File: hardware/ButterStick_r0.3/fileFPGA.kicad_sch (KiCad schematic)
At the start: 20 parts, among them U2 ECP5UM5G_85_CABGA381, U6 S25FL127S, X1 ASDMB

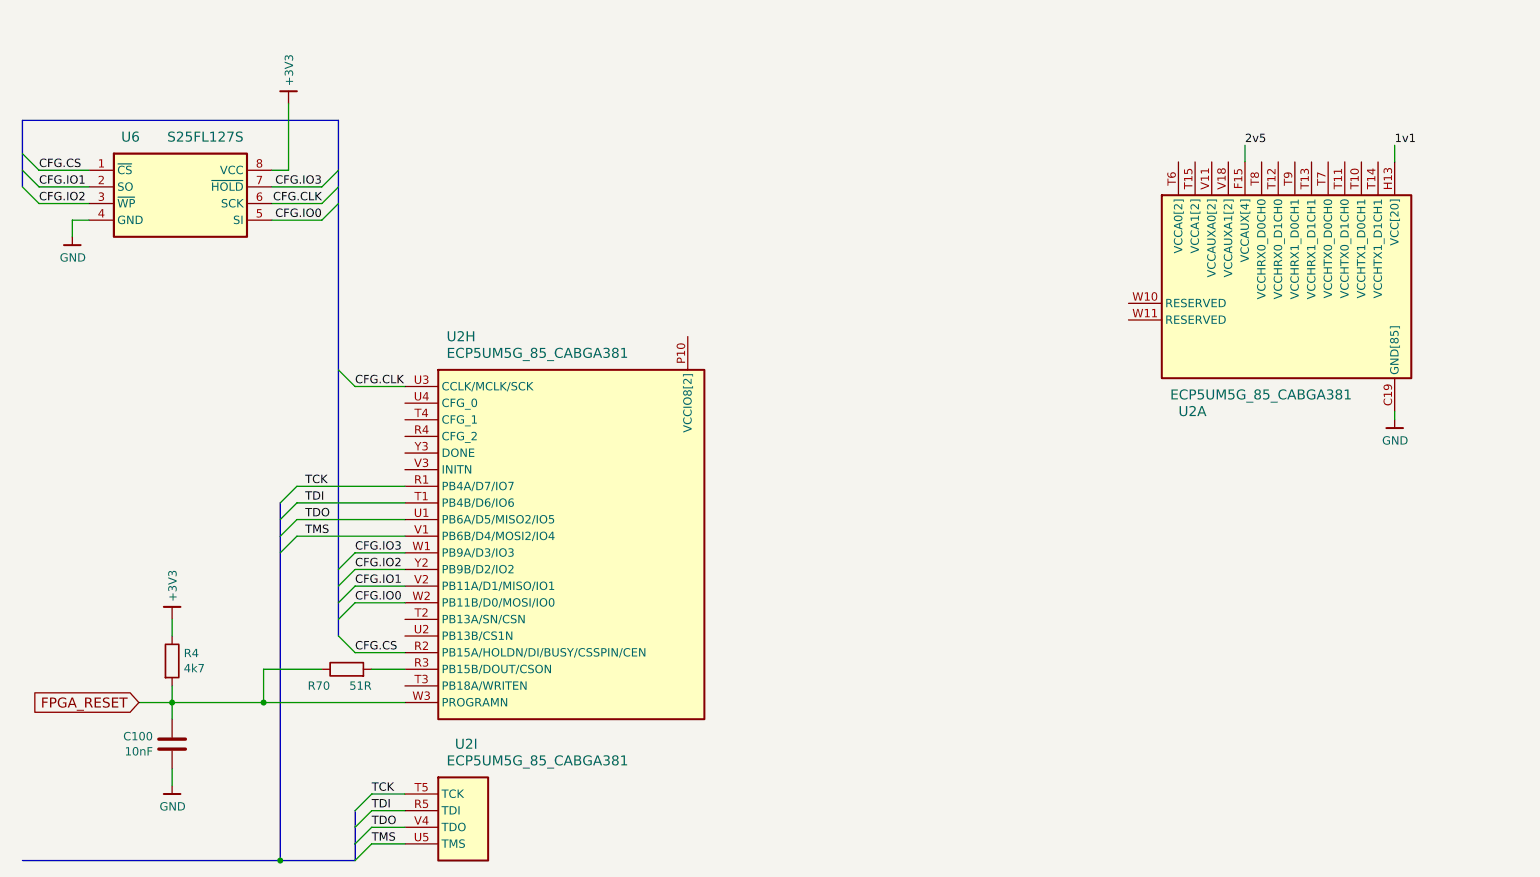
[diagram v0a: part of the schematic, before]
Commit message: hw.r0_3: routing improvements
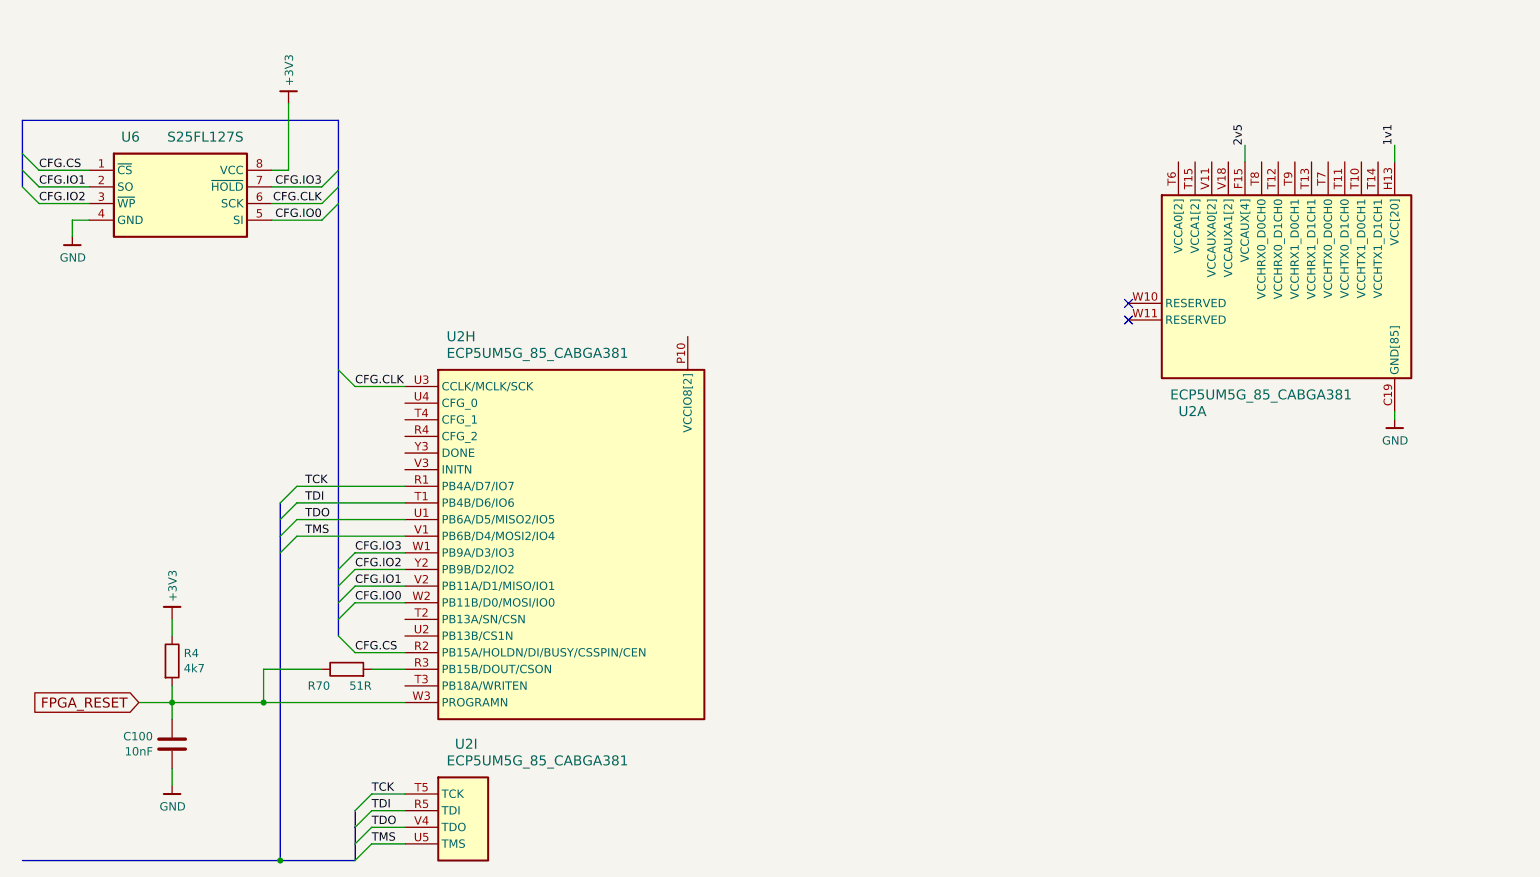
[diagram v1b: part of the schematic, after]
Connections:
- no-connect marks 0 -> 2
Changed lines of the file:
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@@
   (junction (at 502.92 -36.83))
   (junction (at 66.04 166.37))
+  (no_connect (at 195.58 81.28))
+  (no_connect (at 195.58 83.82))
   (bus_entry (at 29.21 60.96) (size -2.54 -2.54))
   (bus_entry (at 29.21 63.5) (size -2.54 -2.54))
@@
   (wire (pts (xy 502.92 -41.91) (xy 502.92 -36.83)))
   (wire (pts (xy 502.92 -36.83) (xy 502.92 -35.56)))
-  (bus (pts (xy 26.67 53.34) (xy 26.67 60.96)))
-  (bus (pts (xy 26.67 60.96) (xy 26.67 63.5)))
+  (bus (pts (xy 26.67 53.34) (xy 26.67 58.42)))
+  (bus (pts (xy 26.67 58.42) (xy 26.67 63.5)))
   (bus (pts (xy 26.67 166.37) (xy 66.04 166.37)))
   (bus (pts (xy 66.04 111.76) (xy 66.04 116.84)))
@@
   (bus (pts (xy 74.93 53.34) (xy 74.93 63.5)))
   (bus (pts (xy 74.93 63.5) (xy 74.93 91.44)))
-  (bus (pts (xy 74.93 91.44) (xy 74.93 121.92)))
-  (bus (pts (xy 74.93 121.92) (xy 74.93 127)))
-  (bus (pts (xy 74.93 127) (xy 74.93 132.08)))
-  (bus (pts (xy 77.47 158.75) (xy 77.47 163.83)))
-  (bus (pts (xy 77.47 163.83) (xy 77.47 166.37)))
+  (bus (pts (xy 74.93 91.44) (xy 74.93 124.46)))
+  (bus (pts (xy 74.93 124.46) (xy 74.93 129.54)))
+  (bus (pts (xy 74.93 129.54) (xy 74.93 132.08)))
+  (bus (pts (xy 77.47 158.75) (xy 77.47 161.29)))
+  (bus (pts (xy 77.47 161.29) (xy 77.47 166.37)))
   (text "LEDS/SDMMC\n" (at 307.34 -17.78 90)
     (effects (font (size 2.54 2.54)) (justify left bottom))
@@
     (effects (font (size 1.27 1.27)) (justify left bottom))
   )
-  (label "2v5" (at 213.36 57.15 0)
-    (effects (font (size 1.27 1.27)) (justify left bottom))
-  )
-  (label "1v1" (at 236.22 57.15 0)
-    (effects (font (size 1.27 1.27)) (justify left bottom))
-  )
+  (label "2v5" (at 213.36 57.15 90)
+    (effects (font (size 1.27 1.27)) (justify left bottom))
+  )
+  (label "1v1" (at 236.22 57.15 90)
+    (effects (font (size 1.27 1.27)) (justify left bottom))
+  )

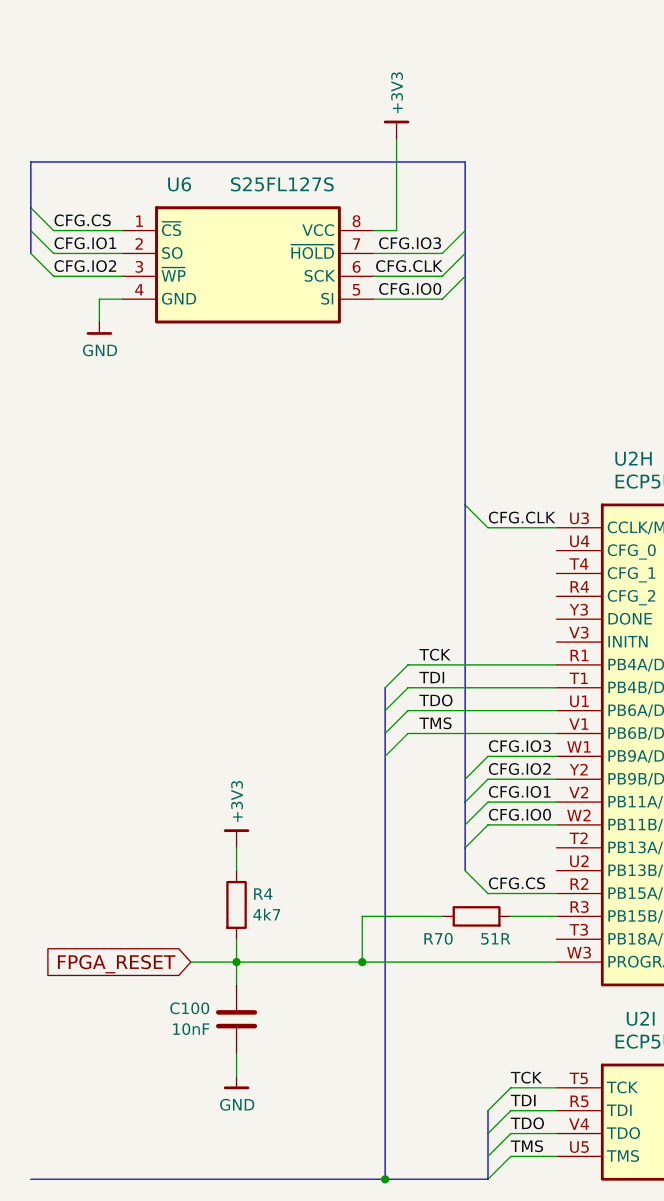
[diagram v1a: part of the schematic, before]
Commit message: hw.r0_3: Start routing DDR3 interface
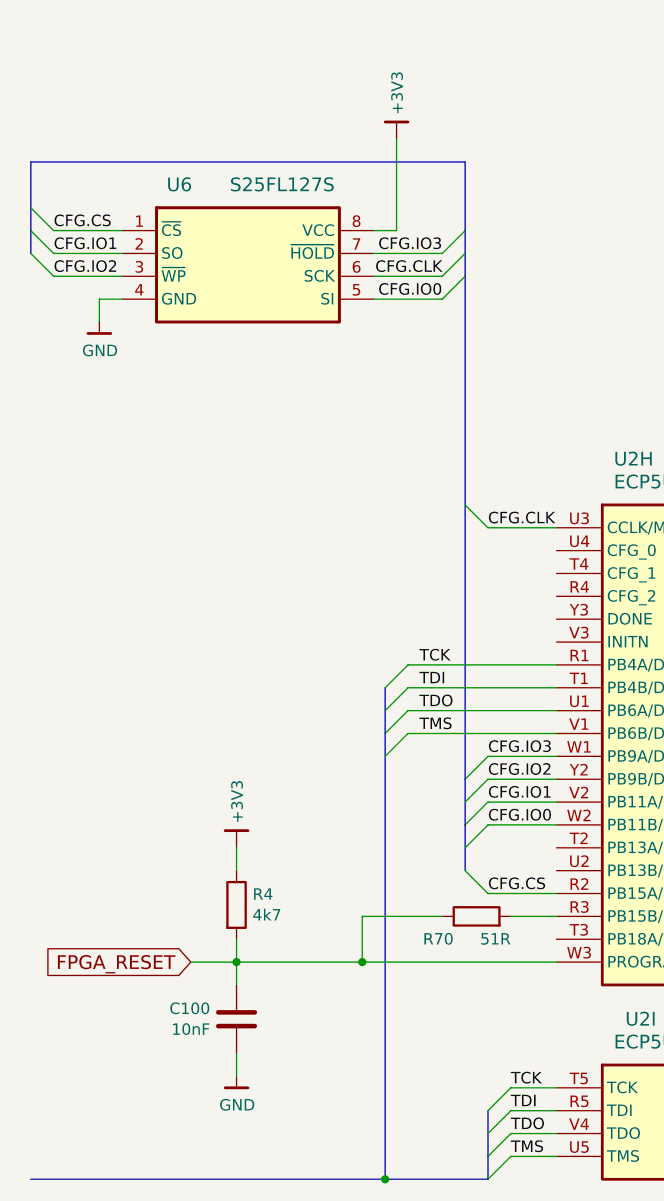
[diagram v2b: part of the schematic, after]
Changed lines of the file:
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@@
-(kicad_sch (version 20200512) (host eeschema "5.99.0-unknown-c8476d6~101~ubuntu18.04.1")
-  (page 8 20)
+(kicad_sch (version 20200512) (host eeschema "5.99.0-unknown-711fc99~101~ubuntu18.04.1")
+  (page 1 20)
   (paper "A4")
   (title_block
@@
   (wire (pts (xy 502.92 -41.91) (xy 502.92 -36.83)))
   (wire (pts (xy 502.92 -36.83) (xy 502.92 -35.56)))
-  (bus (pts (xy 26.67 53.34) (xy 26.67 58.42)))
-  (bus (pts (xy 26.67 58.42) (xy 26.67 63.5)))
+  (bus (pts (xy 26.67 53.34) (xy 26.67 60.96)))
+  (bus (pts (xy 26.67 60.96) (xy 26.67 63.5)))
   (bus (pts (xy 26.67 166.37) (xy 66.04 166.37)))
   (bus (pts (xy 66.04 111.76) (xy 66.04 116.84)))
@@
   (bus (pts (xy 66.04 166.37) (xy 77.47 166.37)))
   (bus (pts (xy 74.93 53.34) (xy 26.67 53.34)))
-  (bus (pts (xy 74.93 53.34) (xy 74.93 63.5)))
-  (bus (pts (xy 74.93 63.5) (xy 74.93 91.44)))
-  (bus (pts (xy 74.93 91.44) (xy 74.93 124.46)))
-  (bus (pts (xy 74.93 124.46) (xy 74.93 129.54)))
-  (bus (pts (xy 74.93 129.54) (xy 74.93 132.08)))
-  (bus (pts (xy 77.47 158.75) (xy 77.47 161.29)))
-  (bus (pts (xy 77.47 161.29) (xy 77.47 166.37)))
+  (bus (pts (xy 74.93 53.34) (xy 74.93 60.96)))
+  (bus (pts (xy 74.93 60.96) (xy 74.93 66.04)))
+  (bus (pts (xy 74.93 66.04) (xy 74.93 121.92)))
+  (bus (pts (xy 74.93 121.92) (xy 74.93 127)))
+  (bus (pts (xy 74.93 127) (xy 74.93 132.08)))
+  (bus (pts (xy 77.47 158.75) (xy 77.47 163.83)))
+  (bus (pts (xy 77.47 163.83) (xy 77.47 166.37)))
   (text "LEDS/SDMMC\n" (at 307.34 -17.78 90)
     (effects (font (size 2.54 2.54)) (justify left bottom))

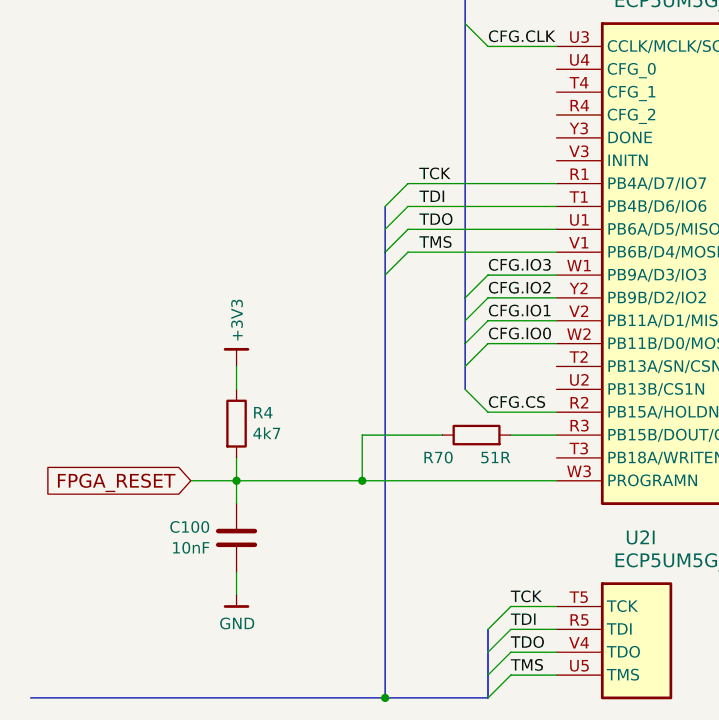
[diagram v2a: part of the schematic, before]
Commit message: hw.r0_3: routed SYZYGY, begin routing RGMII/ULPI
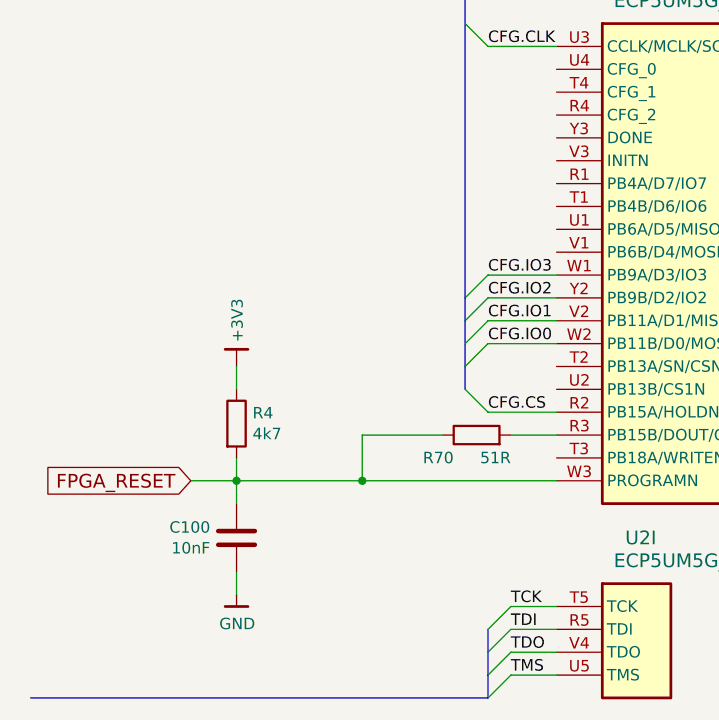
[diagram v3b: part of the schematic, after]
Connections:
- net TCK: no longer U2.R1 (PB4A/D7/IO7)
- net TDI: no longer U2.T1 (PB4B/D6/IO6)
- net TDO: no longer U2.U1 (PB6A/D5/MISO2/IO5)
- net TMS: no longer U2.V1 (PB6B/D4/MOSI2/IO4)
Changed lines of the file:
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@@
 (kicad_sch (version 20200512) (host eeschema "5.99.0-unknown-711fc99~101~ubuntu18.04.1")
-  (page 1 20)
+  (page 1 19)
   (paper "A4")
   (title_block
@@
   (junction (at 63.5 142.24))
   (junction (at 502.92 -36.83))
-  (junction (at 66.04 166.37))
   (no_connect (at 195.58 81.28))
   (no_connect (at 195.58 83.82))
@@
   (bus_entry (at 29.21 63.5) (size -2.54 -2.54))
   (bus_entry (at 29.21 66.04) (size -2.54 -2.54))
-  (bus_entry (at 66.04 111.76) (size 2.54 -2.54))
-  (bus_entry (at 66.04 114.3) (size 2.54 -2.54))
-  (bus_entry (at 66.04 116.84) (size 2.54 -2.54))
-  (bus_entry (at 66.04 119.38) (size 2.54 -2.54))
   (bus_entry (at 72.39 63.5) (size 2.54 -2.54))
   (bus_entry (at 72.39 66.04) (size 2.54 -2.54))
@@
   (wire (pts (xy 64.77 60.96) (xy 67.31 60.96)))
   (wire (pts (xy 67.31 60.96) (xy 67.31 50.8)))
-  (wire (pts (xy 68.58 109.22) (xy 85.09 109.22)))
-  (wire (pts (xy 68.58 111.76) (xy 85.09 111.76)))
-  (wire (pts (xy 68.58 114.3) (xy 85.09 114.3)))
-  (wire (pts (xy 68.58 116.84) (xy 85.09 116.84)))
   (wire (pts (xy 72.39 63.5) (xy 64.77 63.5)))
   (wire (pts (xy 72.39 66.04) (xy 64.77 66.04)))
@@
   (bus (pts (xy 26.67 53.34) (xy 26.67 60.96)))
   (bus (pts (xy 26.67 60.96) (xy 26.67 63.5)))
-  (bus (pts (xy 26.67 166.37) (xy 66.04 166.37)))
-  (bus (pts (xy 66.04 111.76) (xy 66.04 116.84)))
-  (bus (pts (xy 66.04 116.84) (xy 66.04 166.37)))
-  (bus (pts (xy 66.04 166.37) (xy 77.47 166.37)))
+  (bus (pts (xy 26.67 166.37) (xy 77.47 166.37)))
   (bus (pts (xy 74.93 53.34) (xy 26.67 53.34)))
   (bus (pts (xy 74.93 53.34) (xy 74.93 60.96)))
   (bus (pts (xy 74.93 60.96) (xy 74.93 66.04)))
   (bus (pts (xy 74.93 66.04) (xy 74.93 121.92)))
-  (bus (pts (xy 74.93 121.92) (xy 74.93 127)))
-  (bus (pts (xy 74.93 127) (xy 74.93 132.08)))
+  (bus (pts (xy 74.93 121.92) (xy 74.93 124.46)))
+  (bus (pts (xy 74.93 124.46) (xy 74.93 129.54)))
+  (bus (pts (xy 74.93 129.54) (xy 74.93 132.08)))
   (bus (pts (xy 77.47 158.75) (xy 77.47 163.83)))
   (bus (pts (xy 77.47 163.83) (xy 77.47 166.37)))
@@
     (effects (font (size 1.27 1.27)) (justify left bottom))
   )
-  (label "TCK" (at 69.85 109.22 0)
-    (effects (font (size 1.27 1.27)) (justify left bottom))
-  )
-  (label "TDI" (at 69.85 111.76 0)
-    (effects (font (size 1.27 1.27)) (justify left bottom))
-  )
-  (label "TDO" (at 69.85 114.3 0)
-    (effects (font (size 1.27 1.27)) (justify left bottom))
-  )
-  (label "TMS" (at 69.85 116.84 0)
-    (effects (font (size 1.27 1.27)) (justify left bottom))
-  )

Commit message: hw.r0_3: major blocks roughly routed
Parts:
- renumbered C100 to C20, C80 to C21, C81 to C22, C82 to C23, C83 to C24, C84 to C25, C85 to C26, C86 to C27, C87 to C28, C88 to C29, C89 to C30, C90 to C31, C91 to C32, R4 to R41, R70 to R42, R66 to R43, R47 to R44, U2 to U4, U6 to U5

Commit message: hw.r0d3: Length matched all SYZYGY ports
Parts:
- removed X1: ASDMB, Oscillators:Oscillator_SMD_SeikoEpson_SG210-4pin_2.5x2.0mm, symbol gkl_time:TYETBCSANF-32.000000
- added R45, R46, R47, R48, R49: 1K, Resistor_SMD:R_0402_1005Metric, symbol Device:R
- added TP1, TP2, TP3, TP4: TestPoint_Small, gkl_conn:TestPoint_Pad_D1.0mm, symbol Connector:TestPoint_Small
- R44: value 20R -> 1K; PN RMCF0402FT20R0 -> RC0402JR-074K7L; SN-DK (none) -> P10KDECT-ND
- renumbered R41 to R43, R42 to R50, R43 to R51
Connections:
- net PCLKT1_0 is gone; now on net CFG2: R44.2
- net +3V3: now also R44.1, U4.P10 (VCCIO8[2]), U4.P9 (VCCIO8[2]), R46.1, R48.1
- net GND: now also R45.2, R47.2, R49.2
- net TCK: now also TP4.1
- net TDI: now also TP3.1
- net TDO: now also TP2.1
- net TMS: now also TP1.1
- net CFG2: now reaches U4.R4 (CFG_2)
- net CFG2: now also R45.1
- net CFG1: now reaches U4.T4 (CFG_1)
- net CFG1: now also R46.2, R47.1
- net CFG0: now reaches U4.U4 (CFG_0)
- net CFG0: now also R48.2, R49.1
- net 1v1 renamed +1V1
- net 2v5 renamed +2V5
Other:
- moved on the sheet: U4A

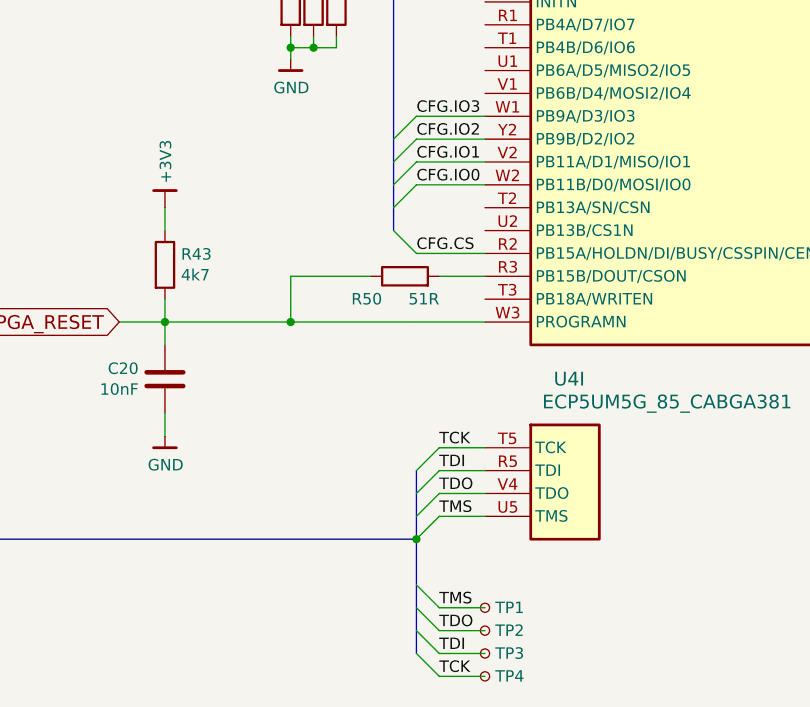
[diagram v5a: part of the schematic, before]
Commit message: hw.r0d3: update routing
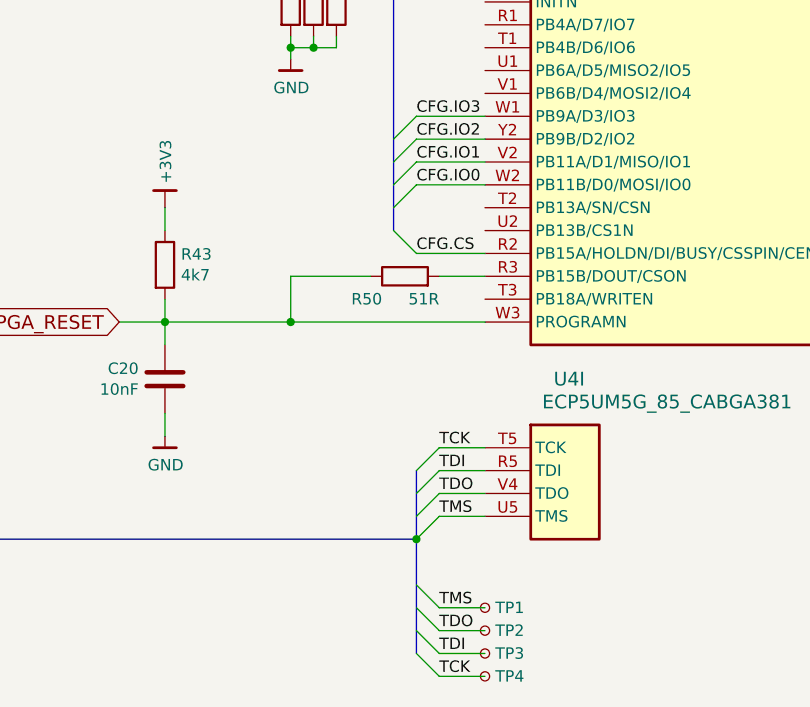
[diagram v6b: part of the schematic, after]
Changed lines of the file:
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@@
 (kicad_sch (version 20200608) (host eeschema "5.99.0-unknown-08c61e6~101~ubuntu18.04.1")
-  (page 7 19)
+  (page 1 19)
   (paper "A4")
   (title_block
@@
     (stroke (width 0) (type solid) (color 0 0 0 0))
   )
-  (bus (pts (xy 74.93 124.46) (xy 74.93 129.54))
-    (stroke (width 0) (type solid) (color 0 0 0 0))
-  )
-  (bus (pts (xy 74.93 129.54) (xy 74.93 132.08))
-    (stroke (width 0) (type solid) (color 0 0 0 0))
-  )
-  (bus (pts (xy 77.47 158.75) (xy 77.47 161.29))
-    (stroke (width 0) (type solid) (color 0 0 0 0))
-  )
-  (bus (pts (xy 77.47 161.29) (xy 77.47 166.37))
-    (stroke (width 0) (type solid) (color 0 0 0 0))
-  )
-  (bus (pts (xy 77.47 166.37) (xy 77.47 173.99))
-    (stroke (width 0) (type solid) (color 0 0 0 0))
-  )
-  (bus (pts (xy 77.47 173.99) (xy 77.47 179.07))
-    (stroke (width 0) (type solid) (color 0 0 0 0))
-  )
+  (bus (pts (xy 74.93 124.46) (xy 74.93 127))
+    (stroke (width 0) (type solid) (color 0 0 0 0))
+  )
+  (bus (pts (xy 74.93 127) (xy 74.93 132.08))
+    (stroke (width 0) (type solid) (color 0 0 0 0))
+  )
+  (bus (pts (xy 77.47 158.75) (xy 77.47 163.83))
+    (stroke (width 0) (type solid) (color 0 0 0 0))
+  )
+  (bus (pts (xy 77.47 163.83) (xy 77.47 166.37))
+    (stroke (width 0) (type solid) (color 0 0 0 0))
+  )
+  (bus (pts (xy 77.47 166.37) (xy 77.47 171.45))
+    (stroke (width 0) (type solid) (color 0 0 0 0))
+  )
+  (bus (pts (xy 77.47 171.45) (xy 77.47 176.53))
+    (stroke (width 0) (type solid) (color 0 0 0 0))
+  )
+  (bus (pts (xy 77.47 176.53) (xy 77.47 179.07))
+    (stroke (width 0) (type solid) (color 0 0 0 0))
+  )
